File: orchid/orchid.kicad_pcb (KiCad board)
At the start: 4 copper layers, 70.7 x 53.3 mm, 144 parts, among them J1 NEIGHBOR1, J10 TEST_2P, J11 TEST_2P, J12 TEST_2P, J13 TEST_2P, J14 TEST_2P, J15 TEST_2P, J16 TEST_2P, J17 Conn_Coaxial, J18 Conn_Coaxial, J19 TEST_2P, J2 NEIGHBOR2, J20 TEST_2P, J21 TEST_2P, J22 TEST_2P, J23 TEST_2P, J24 TEST_2P, J25 TEST_2P, J26 TEST_2P, J27 Conn_01x04, J28 Conn_01x04, J3 Conn_01x06, J4 Conn_01x06, J5 Conn_01x06, J6 Conn_01x06, J7 BONUS_ROW, J8 Conn_01x04, J9 TEST_2P, U1 ADF7242, U2 ADF7242, U3 ADF7242, U4 ADF7242, U5 SKY13322, X1 XTAL4PIN, X2 XTAL4PIN, X3 XTAL4PIN, X4 XTAL4PIN

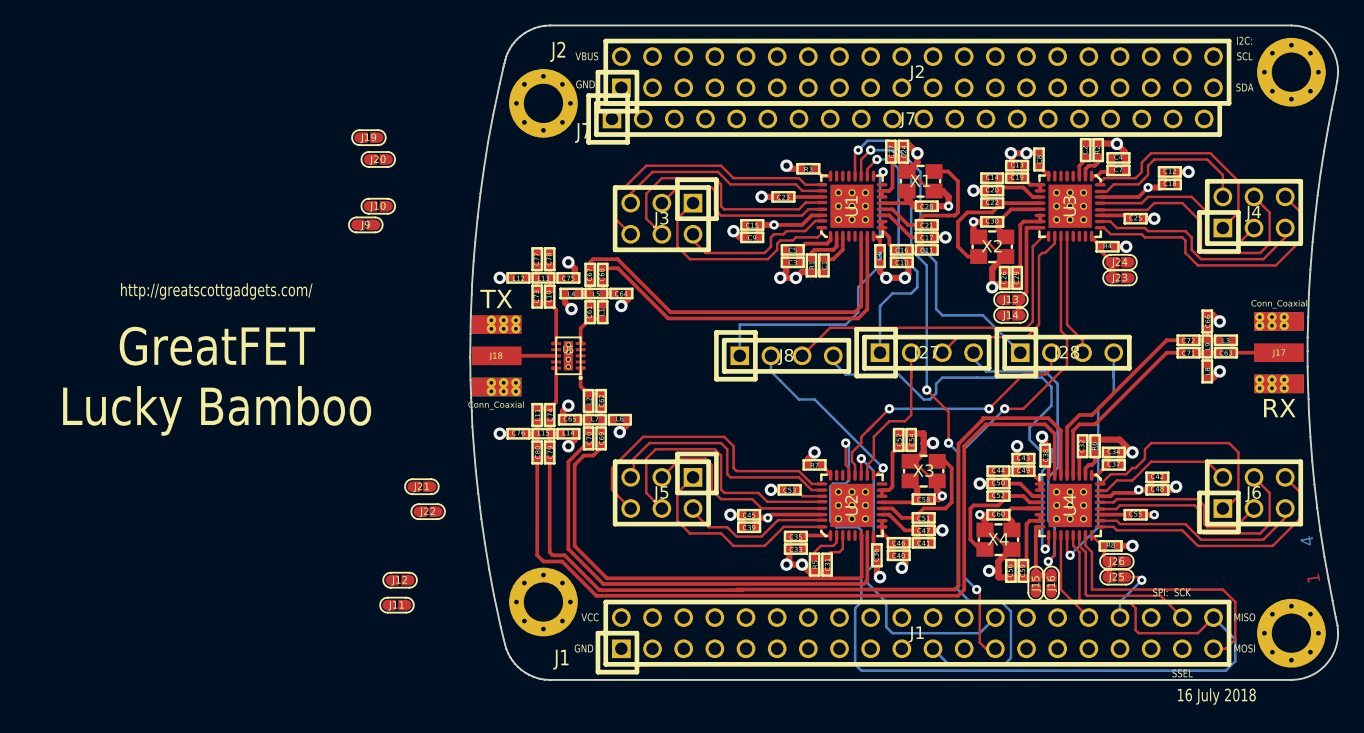
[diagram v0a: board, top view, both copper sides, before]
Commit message: Completed PCB layout
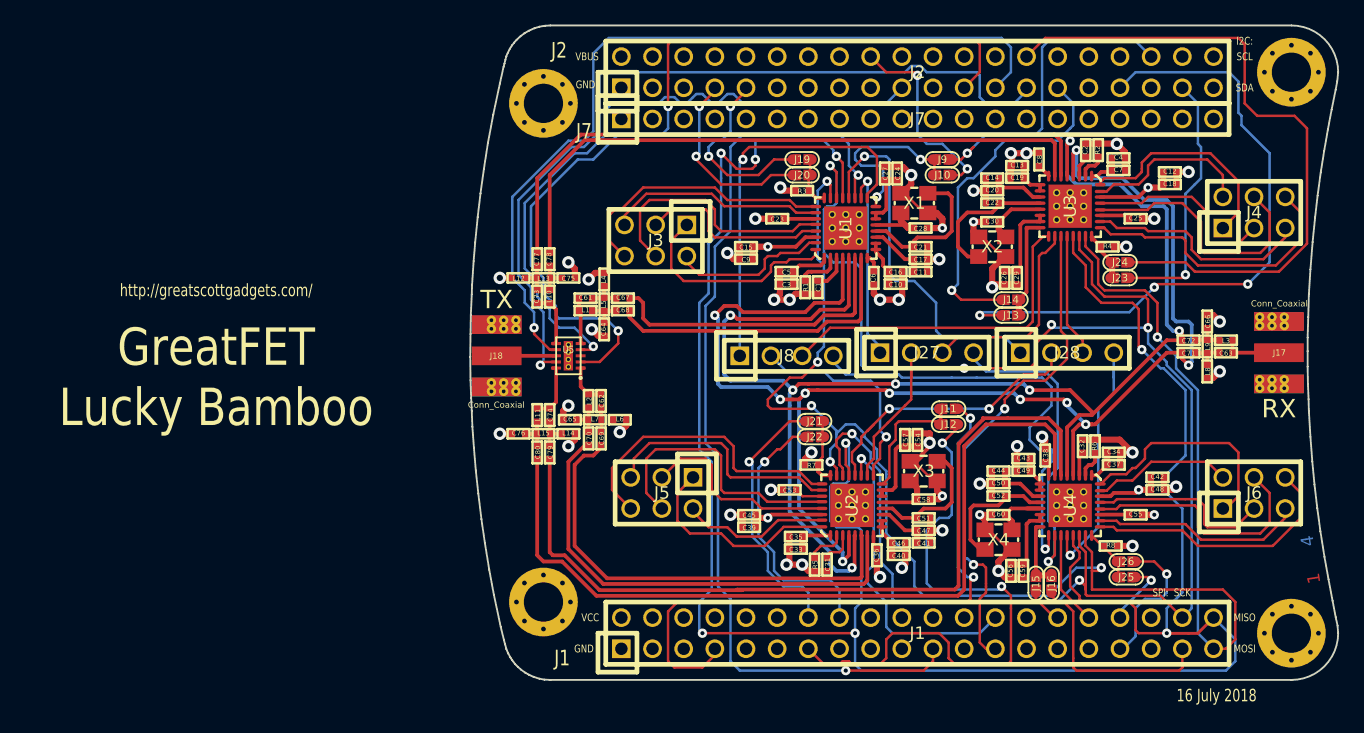
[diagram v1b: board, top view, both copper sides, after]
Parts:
- moved J11 47.7 mm to (148.6, 99.8)
- moved J9 47.3 mm to (148.1, 79.5)
- moved J12 46.5 mm to (148.6, 101.1)
- moved J10 46.0 mm to (148.1, 80.8)
- moved J19 35.4 mm to (136.7, 79.5), turned to 180 degrees
- moved J20 34.6 mm to (136.7, 80.8), turned to 180 degrees
- moved J21 32.4 mm to (137.7, 100.8), turned to 180 degrees
- moved J22 32.1 mm to (137.7, 102.1), turned to 180 degrees
- moved C68 3.36 mm to (122.0, 91.8), turned to 180 degrees
- moved C67 3.28 mm to (122.0, 90.8), turned to 180 degrees
- moved C64 3.24 mm to (120.5, 93.3), turned to 270 degrees
- moved L4 2.90 mm to (120.5, 89.3), turned to 270 degrees
- moved C10 1.85 mm to (144.3, 89.7)
- moved C11 1.85 mm to (146.3, 88.6)
- moved C16 1.85 mm to (144.3, 88.6)
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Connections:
- J10 pad 2: /P1_15 -> /P2_5
- J11 pad 2: /P6_6 -> /P1_0
- J12 pad 2: /P9_5 -> /P1_5
- J14 pad 2: /P1_18 -> /P6_8
- J15 pad 2: /P6_8 -> /P1_16
- J16 pad 2: /P1_6 -> /P1_20
- J19 pad 2: /P1_20 -> /P4_3
- J20 pad 2: /P6_7 -> /P4_4
- J21 pad 2: /P6_0 -> /P5_2
- J22 pad 2: /P3_7 -> /P1_6
- J23 pad 2: /P2_0 -> /P3_5
- J26 pad 2: /P2_3 -> /P9_5
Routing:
- net /P1_19: track 13.7 -> 135.7 mm, vias 0 -> 6
- net /P1_3: track 79.2 -> 193.5 mm, vias 1 -> 8
- net /P1_4: track 21.9 -> 129.7 mm, vias 0 -> 6
- net /RFIN_P: track 15.1 -> 114.9 mm, vias 0 -> 10
- net /RFIN_N: track 16.2 -> 114.5 mm, vias 0 -> 7
- net /P7_2: track 0.00 -> 70.4 mm, vias 0 -> 2
- net /P7_1: track 0.00 -> 68.1 mm, vias 0 -> 1
- net /P7_0: track 0.00 -> 67.4 mm, vias 0 -> 1
- net /P3_4: track 0.00 -> 54.9 mm
- net /P2_4: track 0.00 -> 54.4 mm, vias 0 -> 1
- net /P2_2: track 0.00 -> 53.6 mm, vias 0 -> 3
- net /RFOUT3_P: track 0.00 -> 53.3 mm
- net /P1_0: track 0.00 -> 51.6 mm, vias 0 -> 2
- net /RFOUT3_N: track 0.00 -> 51.5 mm
- net /P1_5: track 0.00 -> 49.0 mm, vias 0 -> 2
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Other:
- board text removed: "SSEL"

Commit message: Added silkscreen labels for headers
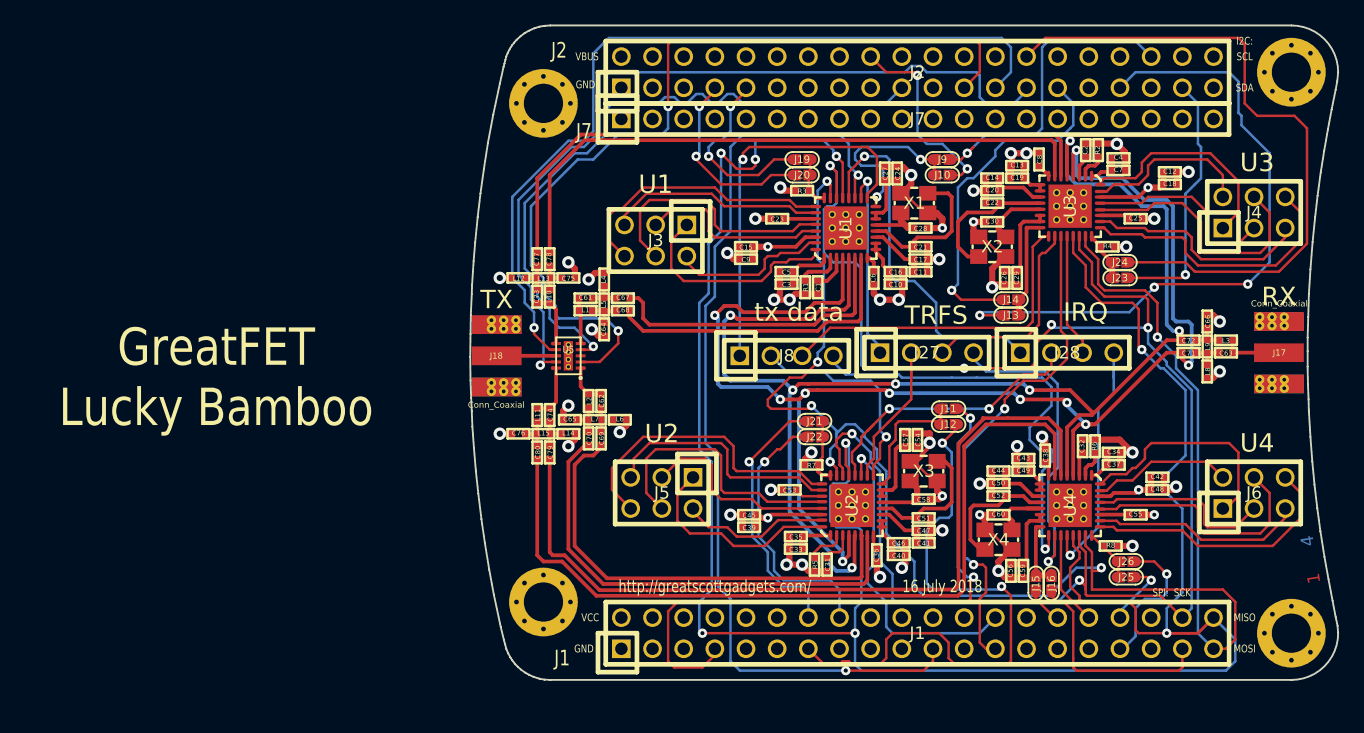
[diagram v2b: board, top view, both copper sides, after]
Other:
- board text added: "IRQ"
- board text added: "TRFS"
- board text added: "U1"
- board text added: "U2"
- board text added: "U3"
- board text added: "U4"
- board text added: "tx data"
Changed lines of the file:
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@@
     (links 469)
     (no_connects 6)
-    (area 109.525999 68.504999 180.415001 121.995001)
+    (area 75.11143 66.04 279.525801 124.460001)
     (thickness 1.6)
-    (drawings 123)
+    (drawings 131)
     (tracks 1706)
     (zones 0)
@@
     (33 F.Adhes user)
     (35 F.Paste user)
+    (36 B.SilkS user)
     (37 F.SilkS user)
     (39 F.Mask user)
     (40 Dwgs.User user)
-    (41 Cmts.User user hide)
+    (41 Cmts.User user)
     (42 Eco1.User user)
     (43 Eco2.User user)
@@
     (pad_to_paste_clearance_ratio -0.05)
     (aux_axis_origin 0 0)
-    (visible_elements FFFFFF7F)
+    (visible_elements FFFCFF7F)
     (pcbplotparams
       (layerselection 0x010a8_80000007)
@@
       (net 164 "Net-(J6-Pad6)"))
   )
-  (gr_text RX (at 175.514 99.822) (layer F.SilkS)
+  (gr_text "GreatFET\nLucky Bamboo" (at 95.25 113.03) (layer B.SilkS)
+    (effects (font (size 3.048 2.54) (thickness 0.4572)) (justify mirror))
+  )
+  (gr_text IRQ (at 159.766 91.948) (layer F.SilkS)
+    (effects (font (size 1.5 1.5) (thickness 0.3)))
+  )
+  (gr_text TRFS (at 147.574 92.202) (layer F.SilkS)
+    (effects (font (size 1.5 1.5) (thickness 0.3)))
+  )
+  (gr_text "tx data" (at 136.398 91.948) (layer F.SilkS)
+    (effects (font (size 1.5 1.5) (thickness 0.3)))
+  )
+  (gr_text U4 (at 173.736 102.616) (layer F.SilkS)
+    (effects (font (size 1.5 1.5) (thickness 0.3)))
+  )
+  (gr_text U3 (at 173.736 79.756) (layer F.SilkS)
+    (effects (font (size 1.5 1.5) (thickness 0.3)))
+  )
+  (gr_text U2 (at 125.222 101.854) (layer F.SilkS)
+    (effects (font (size 1.5 1.5) (thickness 0.3)))
+  )
+  (gr_text U1 (at 124.714 81.534) (layer F.SilkS)
+    (effects (font (size 1.5 1.5) (thickness 0.3)))
+  )
+  (gr_text RX (at 175.514 90.678) (layer F.SilkS)
     (effects (font (size 1.5 1.5) (thickness 0.3)))
   )
@@
   (gr_line (start 177.9016 92.3544) (end 177.8508 94.0054) (angle 90) (layer Edge.Cuts) (width 0.15))
   (gr_line (start 177.9524 90.5002) (end 177.9016 92.3544) (angle 90) (layer Edge.Cuts) (width 0.15))
-  (gr_text "16 July 2018" (at 170.434 123.19) (layer F.SilkS)
+  (gr_text "16 July 2018" (at 148.082 114.3) (layer F.SilkS)
     (effects (font (size 1.016 0.762) (thickness 0.1524)))
   )
@@
     (effects (font (size 1.016 1.016) (thickness 0.1778)))
   )
-  (gr_text http://greatscottgadgets.com/ (at 88.9 90.17) (layer F.SilkS)
+  (gr_text http://greatscottgadgets.com/ (at 129.54 114.3) (layer F.SilkS)
     (effects (font (size 1.016 0.762) (thickness 0.1524)))
   )

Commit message: Added iCE40HX4K-TQ144 symbol to gsg library
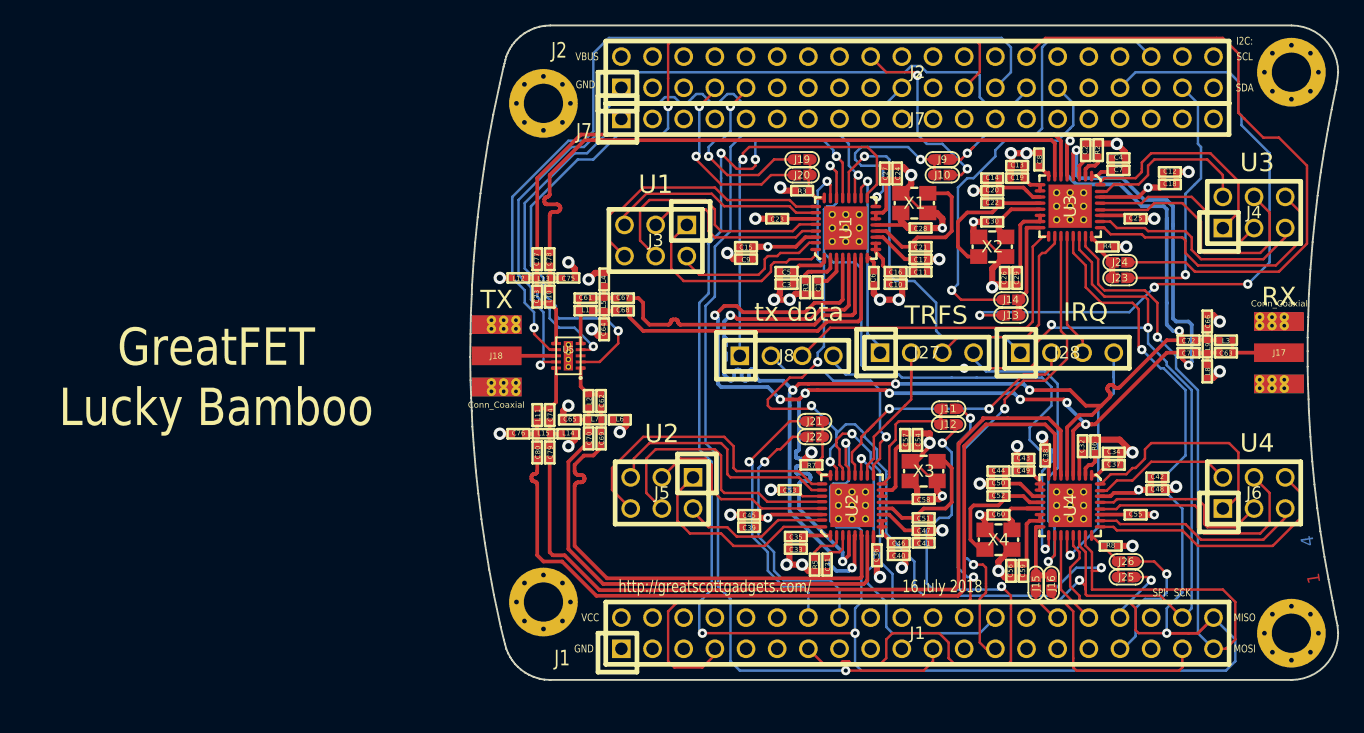
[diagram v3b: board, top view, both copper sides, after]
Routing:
- net /RFIN_N: track 114.5 -> 119.9 mm
- net /RFIN_P: track 114.9 -> 118.2 mm
- net /RFOUT3_N: track 51.5 -> 53.4 mm
- net /P3_4: track 54.9 -> 53.1 mm
- net /RFOUT2_P: track 37.5 -> 38.6 mm
- net /RFOUT4_N: track 67.7 -> 68.3 mm

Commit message: Revised Lucky Bamboo schematic and PCB layout: Added LNA amplifiers on RF input stage and baluns for all RF input/output ports. Added connections from IRQ1/IRQ2 to GreatFET header. Updated GSG Kicad library.
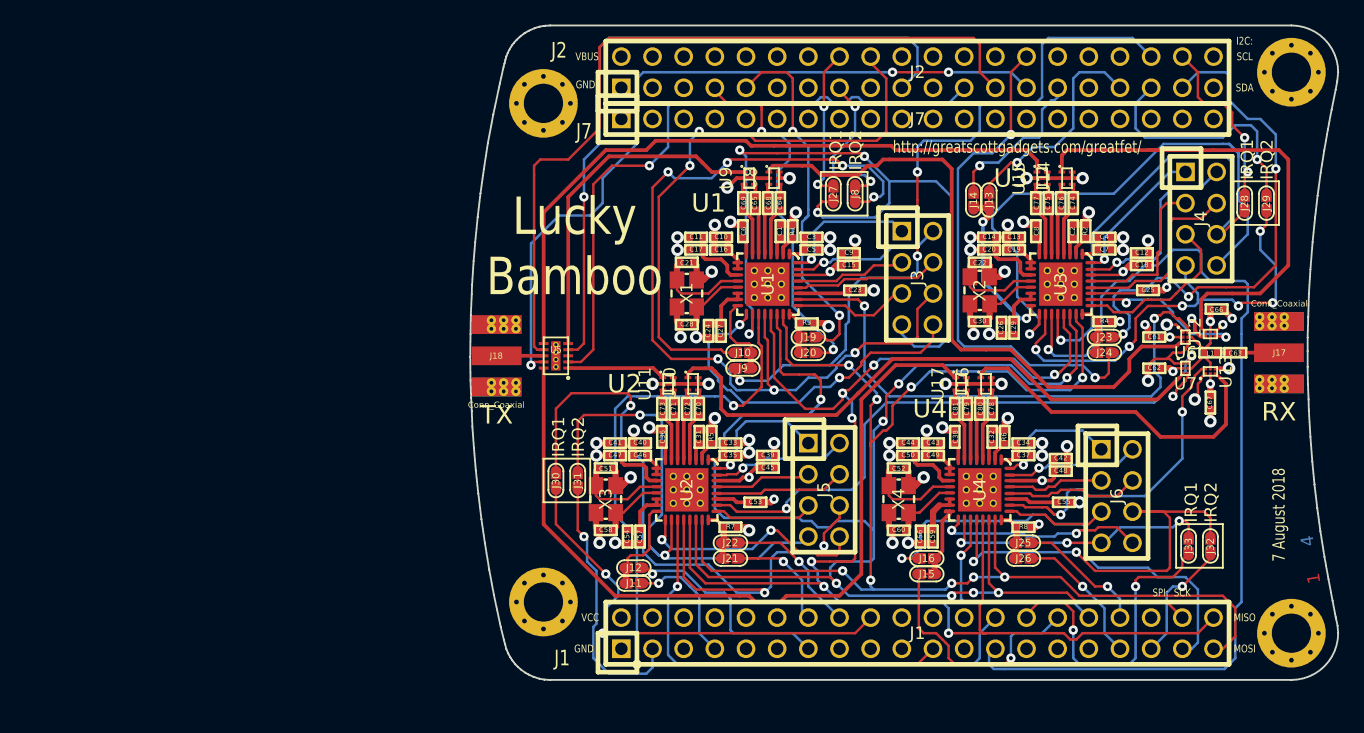
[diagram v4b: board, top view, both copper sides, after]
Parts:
- removed L10, L11, L12, L14, L2, L3, L4, L6, L8: 2n7, gsg-modules:0402
- removed L13, L15, L5, L7, L9: 9n5, gsg-modules:0402
- added C81: 10nF, gsg-modules:0402, F.Cu at (149.1, 99.8)
- added J29: TEST_2P, gsg-modules:0603-JUMPER, F.Cu at (174.5, 83.1)
- added J30: TEST_2P, gsg-modules:0603-JUMPER, F.Cu at (116.6, 105.7)
- added J31: TEST_2P, gsg-modules:0603-JUMPER, F.Cu at (118.4, 105.7)
- added J32: TEST_2P, gsg-modules:0603-JUMPER, F.Cu at (169.9, 111.0)
- added J33: TEST_2P, gsg-modules:0603-JUMPER, F.Cu at (168.1, 111.0)
- added U10: ADF7242_balun, gsg-modules:ADF7242_balun, F.Cu at (127.8, 97.8)
- added U11: ADF7242_balun, gsg-modules:ADF7242_balun, F.Cu at (125.7, 97.8)
- added U12: BGA7H1N6, gsg-modules:TSNP-6-2, F.Cu at (169.9, 93.7)
- added U13: BGA7H1N6, gsg-modules:TSNP-6-2, F.Cu at (169.9, 96.8)
- added U14: ADF7242_balun, gsg-modules:ADF7242_balun, F.Cu at (158.2, 81.0)
- added U15: ADF7242_balun, gsg-modules:ADF7242_balun, F.Cu at (156.2, 81.0)
- added U16: ADF7242_balun, gsg-modules:ADF7242_balun, F.Cu at (151.6, 97.8)
- added U17: ADF7242_balun, gsg-modules:ADF7242_balun, F.Cu at (149.6, 97.8)
- added U6: BGA7H1N6, gsg-modules:TSNP-6-2, F.Cu at (167.9, 94.0)
- added U7: BGA7H1N6, gsg-modules:TSNP-6-2, F.Cu at (167.9, 96.5)
- added U8: ADF7242_balun, gsg-modules:ADF7242_balun, F.Cu at (134.4, 81.0)
- added U9: ADF7242_balun, gsg-modules:ADF7242_balun, F.Cu at (132.3, 81.0)
- C12, C39, C42, C9: value 200nF -> 220nF
- C61, C62, C63, C66: value 1pF -> 1nF
- C64, C65, C73, C74, C75, C76: value 1pF -> 10nF
- C67: value 10nF -> 1nF
- J27, J28, J8: value Conn_01x04 -> TEST_2P; footprint gsg-modules:HEADER-1x4 -> gsg-modules:0603-JUMPER
- J3, J4, J5, J6: value Conn_01x06 -> Conn_01x08; footprint gsg-modules:HEADER-2x3 -> gsg-modules:HEADER-2x4
- L1: value 2n7 -> 3.8nH
- moved L1 51.0 mm to (169.9, 95.2), turned to 0 degrees
- moved C67 48.6 mm to (169.9, 99.3), turned to 270 degrees
- moved C76 48.0 mm to (157.7, 83.1), turned to 90 degrees
- moved C61 46.5 mm to (165.4, 94.0)
- moved C74 46.0 mm to (158.8, 83.1), turned to 270 degrees
- moved C62 45.2 mm to (165.4, 96.5), turned to 180 degrees
- moved C71 42.2 mm to (126.2, 99.8), turned to 270 degrees
- moved C72 41.3 mm to (127.3, 99.8), turned to 90 degrees
- moved C77 40.9 mm to (155.7, 83.1), turned to 90 degrees
- moved C75 39.6 mm to (156.7, 83.1), turned to 270 degrees
- moved C78 38.1 mm to (152.1, 99.8)
- moved C80 36.2 mm to (151.1, 99.8)
- moved C79 34.2 mm to (150.1, 99.8), turned to 270 degrees
- moved J11 29.3 mm to (122.9, 114.0)
- moved J12 28.2 mm to (122.9, 112.8)
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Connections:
- net Net-(J3-Pad1) renamed /PABIAOP1
- net Net-(J3-Pad2) renamed /PAVSUP1
- net Net-(J3-Pad3) renamed /XOSC32KN1
- net Net-(J3-Pad4) renamed /XOSC32KP1
- net Net-(J4-Pad1) renamed /PABIAOP3
- net Net-(J4-Pad2) renamed /PAVSUP3
- net Net-(J4-Pad3) renamed /XOSC32KN3
- net Net-(J4-Pad4) renamed /XOSC32KP3
- net Net-(J5-Pad1) renamed /PABIAOP2
- net Net-(J5-Pad2) renamed /PAVSUP2
- net Net-(J5-Pad3) renamed /XOSC32KN2
- net Net-(J5-Pad4) renamed /XOSC32KP2
- net Net-(J6-Pad1) renamed /PABIAOP4
- net Net-(J6-Pad2) renamed /PAVSUP4
- net Net-(J6-Pad3) renamed /XOSC32KN4
- net Net-(J6-Pad4) renamed /XOSC32KP4
- C61 pad 1: Net-(C61-Pad1) -> VCC
- C61 pad 2: /RFOUT1 -> GND
- C62 pad 1: Net-(C62-Pad1) -> VCC
- C62 pad 2: /RFOUT2 -> GND
- C64 pad 2: GND -> /RFIN1_P
- C65 pad 2: GND -> /RFOUT1_P
- C66 pad 1: Net-(C66-Pad1) -> VCC
- C67 pad 1: /RFOUT1_P -> VCC
- C67 pad 2: Net-(C61-Pad1) -> GND
- C68 pad 1: /RFOUT1_N -> /RFIN1_N
- C68 pad 2: Net-(C64-Pad1) -> Net-(C68-Pad2)
- C69 pad 1: /RFOUT2_P -> /RFOUT1_N
- C69 pad 2: Net-(C62-Pad1) -> Net-(C69-Pad2)
- C70 pad 1: /RFOUT2_N -> Net-(C70-Pad1)
- C70 pad 2: Net-(C65-Pad1) -> /RFIN2_P
- C71 pad 1: /RFIN_P -> Net-(C71-Pad1)
- C71 pad 2: Net-(C63-Pad1) -> /RFOUT2_P
- C72 pad 1: /RFIN_N -> /RFIN2_N
- C72 pad 2: Net-(C66-Pad1) -> Net-(C72-Pad2)
- C73 pad 1: Net-(C73-Pad1) -> /RFOUT2_N
- C73 pad 2: /RFOUT3 -> Net-(C73-Pad2)
- C74 pad 2: /RFOUT4 -> /RFIN3_P
- C75 pad 2: GND -> /RFOUT3_P
- C76 pad 1: Net-(C76-Pad1) -> /RFIN3_N
- C76 pad 2: GND -> Net-(C76-Pad2)
- C77 pad 1: /RFOUT3_P -> /RFOUT3_N
- C77 pad 2: Net-(C73-Pad1) -> Net-(C77-Pad2)
- C78 pad 1: /RFOUT3_N -> Net-(C78-Pad1)
- C78 pad 2: Net-(C75-Pad1) -> /RFIN4_P
- C79 pad 1: /RFOUT4_P -> Net-(C79-Pad1)
- C79 pad 2: Net-(C74-Pad1) -> /RFOUT4_P
- C80 pad 1: /RFOUT4_N -> /RFIN4_N
- C80 pad 2: Net-(C76-Pad1) -> Net-(C80-Pad2)
- J27 pad 1: /TRFS1 -> /P7_7
- J27 pad 2: /TRFS2 -> /TRFS1
- J28 pad 1: /IRQ1 -> /P3_6
- J28 pad 2: /IRQ2 -> /IRQ3
- J3 pad 5: Net-(J3-Pad5) -> /TXEN1
- J3 pad 6: Net-(J3-Pad6) -> /IRQ1
- J4 pad 5: Net-(J4-Pad5) -> /TXEN3
- J4 pad 6: Net-(J4-Pad6) -> /IRQ3
- J5 pad 5: Net-(J5-Pad5) -> /TXEN2
- J5 pad 6: Net-(J5-Pad6) -> /IRQ2
- J6 pad 5: Net-(J6-Pad5) -> /TXEN4
- J6 pad 6: Net-(J6-Pad6) -> /IRQ4
- J8 pad 1: /DT1 -> /P2_6
- J8 pad 2: /DT2 -> /IRQ1
- L1 pad 1: Net-(C64-Pad1) -> /RFIN
- L1 pad 2: /RFOUT1 -> Net-(C63-Pad1)
- U1 pad 25: Net-(J3-Pad6) -> /TXEN1
- U1 pad 26: Net-(J3-Pad5) -> /RXEN1
- U1 pad 4: /RFIN_P -> /RFIN1_P
- U1 pad 5: /RFIN_N -> /RFIN1_N
- U2 pad 25: Net-(J5-Pad6) -> /TXEN2
- U2 pad 26: Net-(J5-Pad5) -> /RXEN2
- U2 pad 4: /RFIN_P -> /RFIN2_P
- U2 pad 5: /RFIN_N -> /RFIN2_N
- U3 pad 25: Net-(J4-Pad6) -> /TXEN3
- U3 pad 26: Net-(J4-Pad5) -> /RXEN3
- U3 pad 4: /RFIN_P -> /RFIN3_P
- U3 pad 5: /RFIN_N -> /RFIN3_N
- U4 pad 25: Net-(J6-Pad6) -> /TXEN4
- U4 pad 26: Net-(J6-Pad5) -> /RXEN4
- U4 pad 4: /RFIN_P -> /RFIN4_P
- U4 pad 5: /RFIN_N -> /RFIN4_N
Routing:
- net /RFIN_N: track 119.9 -> 0.00 mm, vias 7 -> 0
- net /RFIN_P: track 118.2 -> 0.00 mm, vias 10 -> 0
- net /RFIN1: track 0.00 -> 82.0 mm
- net /P1_3: track 193.5 -> 119.0 mm, vias 8 -> 7
- net /RFIN2: track 0.00 -> 64.5 mm
- net /RFOUT4_P: track 68.2 -> 3.73 mm
- net /RFOUT4_N: track 68.3 -> 3.94 mm
- net /RFOUT4: track 4.78 -> 65.8 mm
- net /RFIN3: track 0.00 -> 58.0 mm
- net /RFIN4: track 0.00 -> 54.7 mm
- net /RFOUT3: track 4.78 -> 54.9 mm
- net /RFOUT3_P: track 53.3 -> 3.73 mm
- net /RFOUT3_N: track 53.4 -> 3.94 mm
- net /RXEN2: track 0.00 -> 48.2 mm, vias 0 -> 2
- net /TRFS1: track 16.0 -> 63.1 mm, vias 1 -> 4
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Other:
- board text added: "7 August 2018"
- board text added: "IRQ1 IRQ2"
- board text added: "Lucky Bamboo"
- board text added: "http://greatscottgadgets.com/greatfet/"
- board text removed: "16 July 2018"
- board text removed: "GreatFET Lucky Bamboo"
- board text removed: "IRQ"
- board text removed: "TRFS"
- board text removed: "http://greatscottgadgets.com/"
- board text removed: "tx data"
